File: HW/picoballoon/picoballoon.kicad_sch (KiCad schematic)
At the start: 23 parts, among them J1 EXT_DEBUGGER

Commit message: aprs test board
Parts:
- added R10, R11, R12, R13: 10k, symbol Device:R
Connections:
- net +3.3V: now also R10.1, R11.1, R12.1, R13.1
- net GNSS_EXTINT: now also MCXL14x2.5 (P0_13); no longer MCXL14x2.45 (P1_1)
- net GNSS_RESET: now also MCXL14x2.4 (P0_12); no longer MCXL14x2.44 (P1_0)
- net SCLK: now also MCXL14x2.45 (P1_1); no longer MCXL14x2.54 (P1_17)
- net nIRQ: now also MCXL14x2.48 (P1_12); no longer MCXL14x2.57 (P1_20)
- net nSEL: now also MCXL14x2.44 (P1_0); no longer MCXL14x2.56 (P1_19)
- net SDA_TEMP: now reaches MCXL14x2.10 (P0_18)
- net SDA_TEMP: now also R10.2
- net SCL_TEMP: now reaches MCXL14x2.11 (P0_19)
- net SCL_TEMP: now also R11.2
- net LED: now reaches D2.1 (K), MCXL14x2.16 (P0_20)
- net MI: now reaches MCXL14x2.46 (P1_2)
- net MO: now reaches MCXL14x2.47 (P1_3)
- net MO: now also R9.2
- net GNSS_TX: now reaches MCXL14x2.61 (P0_0)
- net GNSS_RX: now reaches MCXL14x2.62 (P0_1)
- net SCL renamed GNSS_SCL
- net SDA renamed GNSS_SDA
- net SI: no longer names the net of MCXL14x2.53 (P1_16)
- net SO: no longer names the net of MCXL14x2.55 (P1_18)
- net SO: no longer R9.2
- new net SCL_SENS: MCXL14x2.57 (P1_20), R13.2
- new net SDA_SENS: MCXL14x2.56 (P1_19), R12.2
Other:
- sheet GNSS ports: added EN, EXTINT, RESET, RX, TX; removed GNSS_EN, GNSS_EXTINT, GNSS_RESET
- sheet sensors ports: added SCL_TEMP, SDA_TEMP; removed none
- moved on the sheet: D2, J1, R1, R3, R4, R5, R9

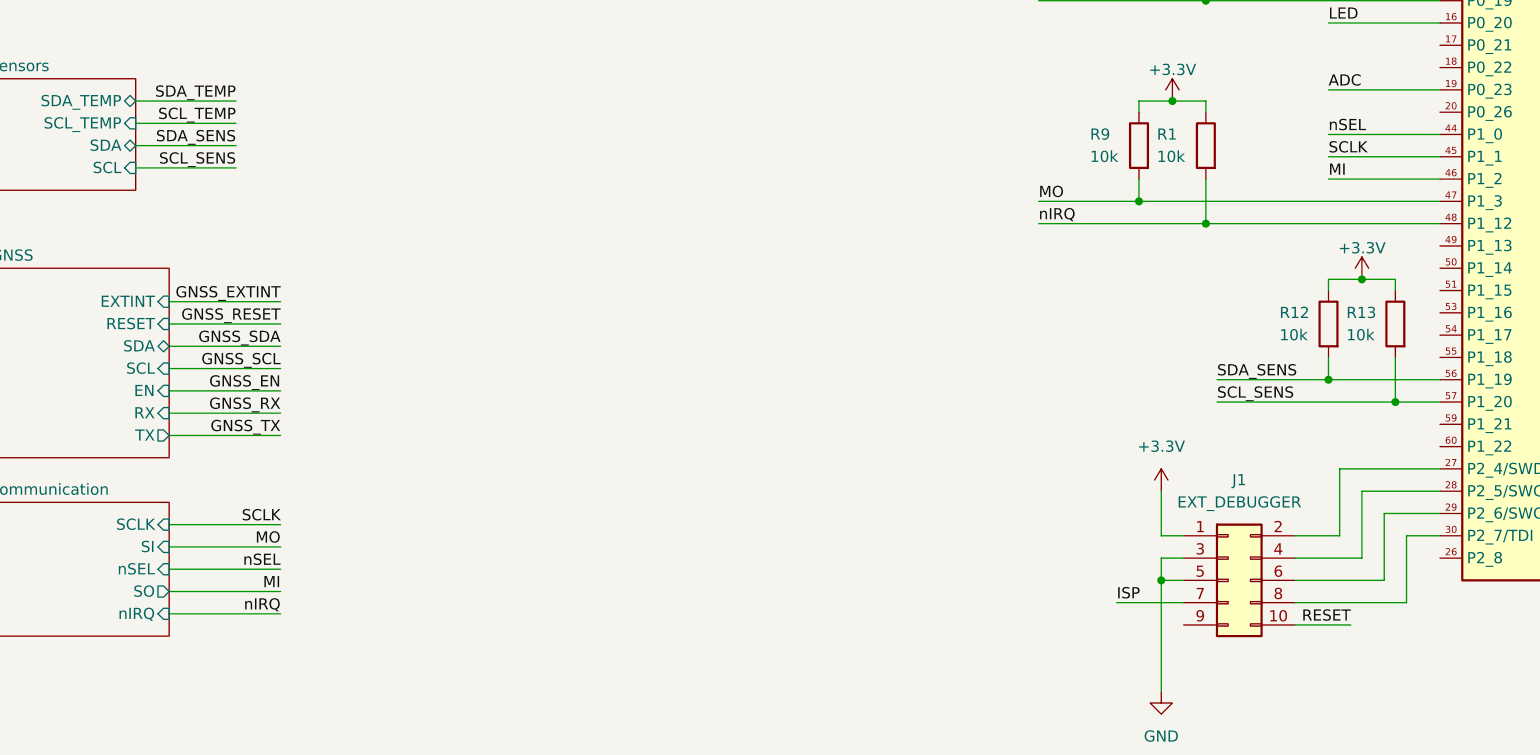
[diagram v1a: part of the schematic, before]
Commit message: some devices replaced
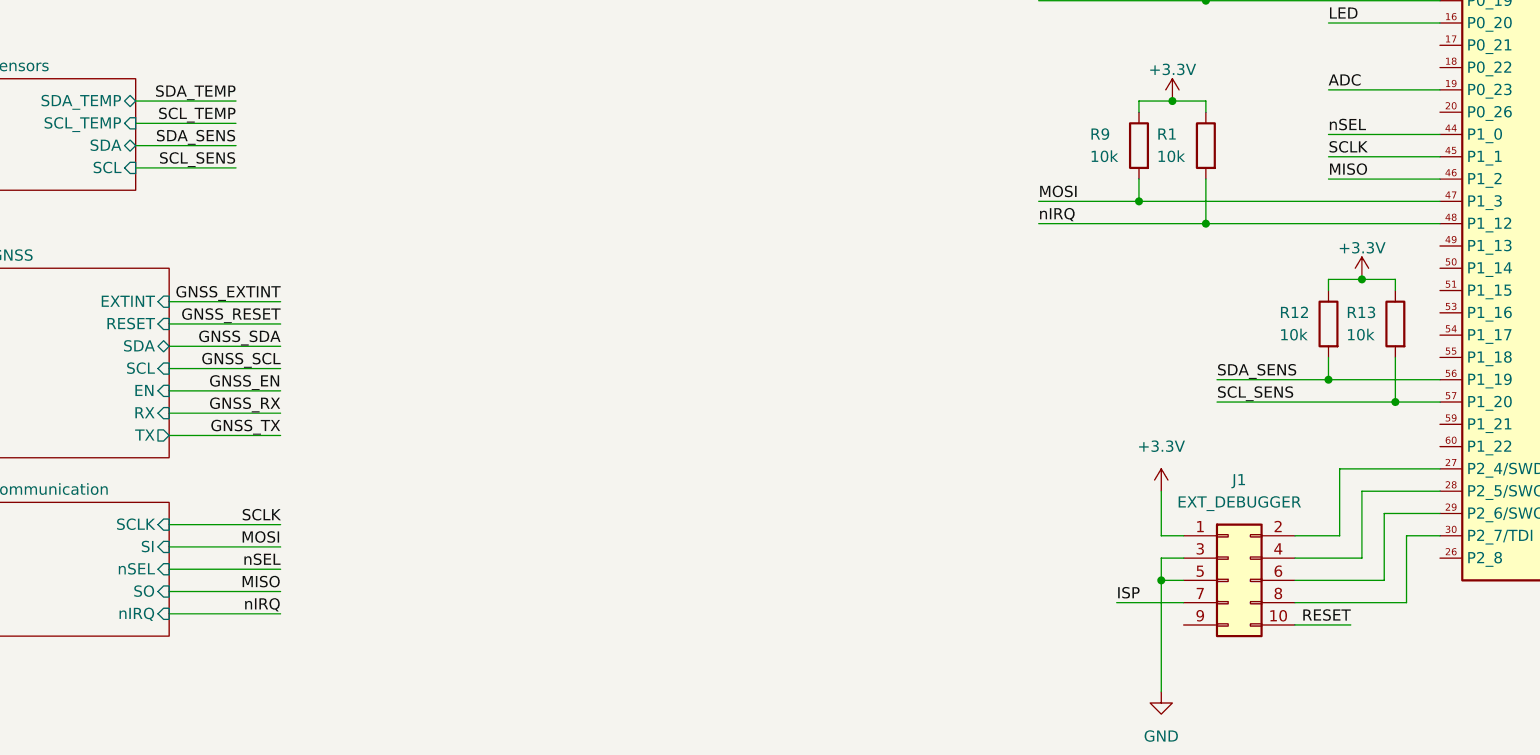
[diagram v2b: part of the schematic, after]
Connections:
- net MI renamed MISO
- net MO renamed MOSI
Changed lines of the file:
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@@
 	(wire
 		(pts
-			(xy 45.72 135.89) (xy 58.42 135.89)
-		)
-		(stroke
-			(width 0)
-			(type default)
-		)
-	)
-	(wire
-		(pts
 			(xy 120.65 170.18) (xy 120.65 168.91)
 		)
@@
 	(wire
 		(pts
+			(xy 45.72 130.81) (xy 58.42 130.81)
+		)
+		(stroke
+			(width 0)
+			(type default)
+		)
+	)
+	(wire
+		(pts
 			(xy 177.8 40.64) (xy 190.5 40.64)
 		)
@@
 	(wire
 		(pts
-			(xy 45.72 130.81) (xy 58.42 130.81)
-		)
-		(stroke
-			(width 0)
-			(type default)
-		)
-	)
-	(wire
-		(pts
 			(xy 259.08 124.46) (xy 275.59 124.46)
 		)
@@
 	(wire
 		(pts
+			(xy 45.72 135.89) (xy 58.42 135.89)
+		)
+		(stroke
+			(width 0)
+			(type default)
+		)
+	)
+	(wire
+		(pts
 			(xy 144.78 68.58) (xy 163.83 68.58)
 		)
@@
 		)
 	)
-	(label "MO"
+	(label "MOSI"
 		(at 58.42 130.81 180)
 		(fields_autoplaced yes)
@@
 		)
 	)
-	(label "MI"
+	(label "MISO"
 		(at 58.42 135.89 180)
 		(fields_autoplaced yes)
@@
 		)
 	)
-	(label "MO"
+	(label "MOSI"
 		(at 144.78 91.44 0)
 		(fields_autoplaced yes)
@@
 		)
 	)
-	(label "MI"
+	(label "MISO"
 		(at 177.8 88.9 0)
 		(fields_autoplaced yes)
@@
 			)
 		)
-		(pin "SO" output
+		(pin "SO" input
 			(at 45.72 135.89 0)
 			(effects

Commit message: pcb
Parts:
- C18, C19, C20, C21, C22, C23, C24, C25, C26, C27, C28, C29: footprint (none) -> Capacitor_SMD:C_0603_1608Metric_Pad1.08x0.95mm_HandSolder
- D2: footprint (none) -> LED_SMD:LED_0603_1608Metric_Pad1.05x0.95mm_HandSolder
- FB3: footprint (none) -> Library:BLM21AG102BH1J
- J1: footprint (none) -> Connector_PinHeader_1.27mm:PinHeader_2x05_P1.27mm_Vertical
- L4, L5: footprint (none) -> Inductor_SMD:L_0603_1608Metric_Pad1.05x0.95mm_HandSolder
- MCXL14x2: footprint (none) -> Package_QFP:LQFP-64-1EP_10x10mm_P0.5mm_EP5x5mm
- R1, R10, R11, R12, R13, R3, R4, R5, R9: footprint (none) -> Resistor_SMD:R_0603_1608Metric_Pad0.98x0.95mm_HandSolder
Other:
- sheet GNSS ports: added none; removed EN
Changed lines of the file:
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@@
 	(wire
 		(pts
-			(xy 45.72 115.57) (xy 58.42 115.57)
+			(xy 45.72 113.03) (xy 58.42 113.03)
 		)
 		(stroke
@@
 	(wire
 		(pts
-			(xy 128.27 55.88) (xy 134.62 55.88)
+			(xy 45.72 115.57) (xy 58.42 115.57)
 		)
 		(stroke
@@
 	(wire
 		(pts
-			(xy 156.21 91.44) (xy 190.5 91.44)
+			(xy 128.27 55.88) (xy 134.62 55.88)
 		)
 		(stroke
@@
 	(wire
 		(pts
-			(xy 186.69 129.54) (xy 190.5 129.54)
+			(xy 156.21 91.44) (xy 190.5 91.44)
 		)
 		(stroke
@@
 	(wire
 		(pts
-			(xy 45.72 102.87) (xy 58.42 102.87)
+			(xy 186.69 129.54) (xy 190.5 129.54)
 		)
 		(stroke
@@
 	(wire
 		(pts
-			(xy 233.68 55.88) (xy 234.95 55.88)
+			(xy 45.72 102.87) (xy 58.42 102.87)
 		)
 		(stroke
@@
 	(wire
 		(pts
-			(xy 45.72 118.11) (xy 58.42 118.11)
+			(xy 233.68 55.88) (xy 234.95 55.88)
 		)
 		(stroke
@@
 	(wire
 		(pts
-			(xy 45.72 113.03) (xy 58.42 113.03)
-		)
-		(stroke
-			(width 0)
-			(type default)
-		)
-	)
-	(wire
-		(pts
 			(xy 233.68 127) (xy 240.03 127)
 		)
@@
 		)
 	)
-	(label "GNSS_EN"
-		(at 58.42 113.03 180)
-		(fields_autoplaced yes)
-		(effects
-			(font
-				(size 1.27 1.27)
-			)
-			(justify right bottom)
-		)
-	)
 	(label "MOSI"
 		(at 58.42 130.81 180)
@@
 	)
 	(label "GNSS_TX"
-		(at 58.42 118.11 180)
+		(at 58.42 115.57 180)
 		(fields_autoplaced yes)
 		(effects
@@
 	)
 	(label "GNSS_RX"
-		(at 58.42 115.57 180)
+		(at 58.42 113.03 180)
 		(fields_autoplaced yes)
 		(effects
@@
 			)
 		)
-		(property "Footprint" ""
+		(property "Footprint" "Package_QFP:LQFP-64-1EP_10x10mm_P0.5mm_EP5x5mm"
 			(at 232.41 62.23 90)
 			(effects
@@
 			)
 		)
-		(property "Footprint" ""
+		(property "Footprint" "LED_SMD:LED_0603_1608Metric_Pad1.05x0.95mm_HandSolder"
 			(at 128.27 46.99 0)
 			(effects
@@
 			)
 		)
-		(property "Footprint" ""
+		(property "Footprint" "Capacitor_SMD:C_0603_1608Metric_Pad1.08x0.95mm_HandSolder"
 			(at 60.6552 177.8 0)
 			(effects
@@
 			)
 		)
-		(property "Footprint" ""
+		(property "Footprint" "Resistor_SMD:R_0603_1608Metric_Pad0.98x0.95mm_HandSolder"
 			(at 130.048 36.83 90)
 			(effects
@@
 			)
 		)
-		(property "Footprint" ""
+		(property "Footprint" "Resistor_SMD:R_0603_1608Metric_Pad0.98x0.95mm_HandSolder"
 			(at 171.958 41.91 90)
 			(effects
@@
 			)
 		)
-		(property "Footprint" ""
+		(property "Footprint" "Resistor_SMD:R_0603_1608Metric_Pad0.98x0.95mm_HandSolder"
 			(at 157.988 59.69 90)
 			(effects
@@
 			)
 		)
-		(property "Footprint" ""
+		(property "Footprint" "Capacitor_SMD:C_0603_1608Metric_Pad1.08x0.95mm_HandSolder"
 			(at 147.0152 177.8 0)
 			(effects
@@
 			)
 		)
-		(property "Footprint" ""
+		(property "Footprint" "Capacitor_SMD:C_0603_1608Metric_Pad1.08x0.95mm_HandSolder"
 			(at 98.7552 177.8 0)
 			(effects
@@
 			)
 		)
-		(property "Footprint" ""
+		(property "Footprint" "Capacitor_SMD:C_0603_1608Metric_Pad1.08x0.95mm_HandSolder"
 			(at 73.3552 177.8 0)
 			(effects
@@
 			)
 		)
-		(property "Footprint" ""
+		(property "Footprint" "Resistor_SMD:R_0603_1608Metric_Pad0.98x0.95mm_HandSolder"
 			(at 179.578 105.41 90)
 			(effects
@@
 			)
 		)
-		(property "Footprint" ""
+		(property "Footprint" "Capacitor_SMD:C_0603_1608Metric_Pad1.08x0.95mm_HandSolder"
 			(at 22.5552 177.8 0)
 			(effects
@@
 			)
 		)
-		(property "Footprint" ""
+		(property "Footprint" "Connector_PinHeader_1.27mm:PinHeader_2x05_P1.27mm_Vertical"
 			(at 166.37 134.62 0)
 			(effects
@@
 			)
 		)
-		(property "Footprint" ""
+		(property "Footprint" "Inductor_SMD:L_0603_1608Metric_Pad1.05x0.95mm_HandSolder"
 			(at 254 104.14 0)
 			(effects
@@
 			)
 		)
-		(property "Footprint" ""
+		(property "Footprint" "Capacitor_SMD:C_0603_1608Metric_Pad1.08x0.95mm_HandSolder"
 			(at 86.0552 177.8 0)
 			(effects
@@
 			)
 		)
-		(property "Footprint" ""
+		(property "Footprint" "Capacitor_SMD:C_0603_1608Metric_Pad1.08x0.95mm_HandSolder"
 			(at 159.7152 177.8 0)
 			(effects
@@
 			)
 		)
-		(property "Footprint" ""
+		(property "Footprint" "Capacitor_SMD:C_0603_1608Metric_Pad1.08x0.95mm_HandSolder"
 			(at 47.9552 177.8 0)
 			(effects
@@
 			)
 		)
-		(property "Footprint" ""
+		(property "Footprint" "Capacitor_SMD:C_0603_1608Metric_Pad1.08x0.95mm_HandSolder"
 			(at 260.0452 113.03 0)
 			(effects
@@
 			)
 		)
-		(property "Footprint" ""
+		(property "Footprint" "Capacitor_SMD:C_0603_1608Metric_Pad1.08x0.95mm_HandSolder"
 			(at 121.6152 177.8 0)
 			(effects
@@
 			)
 		)
-		(property "Footprint" ""
+		(property "Footprint" "Library:BLM21AG102BH1J"
 			(at 133.35 170.688 90)
 			(effects
@@
 			)
 		)
-		(property "Footprint" ""
+		(property "Footprint" "Capacitor_SMD:C_0603_1608Metric_Pad1.08x0.95mm_HandSolder"
 			(at 35.2552 177.8 0)
 			(effects
@@
 			)
 		)
-		(property "Footprint" ""
+		(property "Footprint" "Resistor_SMD:R_0603_1608Metric_Pad0.98x0.95mm_HandSolder"
 			(at 165.608 85.09 90)
 			(effects
@@
 			)
 		)
-		(property "Footprint" ""
+		(property "Footprint" "Resistor_SMD:R_0603_1608Metric_Pad0.98x0.95mm_HandSolder"
 			(at 164.338 41.91 90)
 			(effects
@@
 			)
 		)
-		(property "Footprint" ""
+		(property "Footprint" "Resistor_SMD:R_0603_1608Metric_Pad0.98x0.95mm_HandSolder"
 			(at 157.988 85.09 90)
 			(effects
@@
 			)
 		)
-		(property "Footprint" ""
+		(property "Footprint" "Resistor_SMD:R_0603_1608Metric_Pad0.98x0.95mm_HandSolder"
 			(at 187.198 105.41 90)
 			(effects
@@
 			)
 		)
-		(property "Footprint" ""
+		(property "Footprint" "Resistor_SMD:R_0603_1608Metric_Pad0.98x0.95mm_HandSolder"
 			(at 165.608 59.69 90)
 			(effects
@@
 			)
 		)
-		(property "Footprint" ""
+		(property "Footprint" "Capacitor_SMD:C_0603_1608Metric_Pad1.08x0.95mm_HandSolder"
 			(at 260.0452 133.35 0)
 			(effects
@@
 			)
 		)
-		(property "Footprint" ""
+		(property "Footprint" "Inductor_SMD:L_0603_1608Metric_Pad1.05x0.95mm_HandSolder"
 			(at 254 124.46 0)
 			(effects
@@
 	(sheet
 		(at 25.4 99.06)
-		(size 20.32 21.59)
+		(size 20.32 20.32)
 		(fields_autoplaced yes)
 		(stroke
@@
 		)
 		(property "Sheetfile" "GNSS.kicad_sch"
-			(at 25.4 121.2346 0)
+			(at 25.4 119.9646 0)
 			(effects
 				(font
@@
 			)
 		)
-		(pin "EN" input
-			(at 45.72 113.03 0)
-			(effects
-				(font
-					(size 1.27 1.27)
-				)
-				(justify right)
-			)
-		)
 		(pin "EXTINT" input
 			(at 45.72 102.87 0)
@@
 		)
 		(pin "TX" output
-			(at 45.72 118.11 0)
+			(at 45.72 115.57 0)
 			(effects
 				(font
@@
 		)
 		(pin "RX" input
-			(at 45.72 115.57 0)
+			(at 45.72 113.03 0)
 			(effects
 				(font

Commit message: picoballoon pcb
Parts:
- added C12: 100n, Capacitor_SMD:C_0603_1608Metric_Pad1.08x0.95mm_HandSolder, symbol Device:C
- added R6: 10k, Resistor_SMD:R_0603_1608Metric_Pad0.98x0.95mm_HandSolder, symbol Device:R
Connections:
- net +3.3V: now also R6.1
- net GND: now also C12.2
- net RESET: now also C12.1, R6.2

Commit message: test points
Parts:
- added TP1: +3.3VA_TP, TestPoint:TestPoint_Pad_D2.0mm, symbol Connector:TestPoint
- added TP10, TP9: GND, TestPoint:TestPoint_Pad_D2.0mm, symbol Connector:TestPoint
- added TP2: +3.3V_TP, TestPoint:TestPoint_Pad_D2.0mm, symbol Connector:TestPoint
- added TP4: SDA_TEMP, TestPoint:TestPoint_Pad_D2.0mm, symbol Connector:TestPoint
- added TP5: SCL_TEMP, TestPoint:TestPoint_Pad_D2.0mm, symbol Connector:TestPoint
- added TP6: SCLK, TestPoint:TestPoint_Pad_D2.0mm, symbol Connector:TestPoint
- added TP7: MOSI, TestPoint:TestPoint_Pad_D2.0mm, symbol Connector:TestPoint
- added TP8: MISO, TestPoint:TestPoint_Pad_D2.0mm, symbol Connector:TestPoint
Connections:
- net +3.3V: now also TP2.1
- net +3.3VA: now also TP1.1
- net GND: now also TP10.1, TP9.1
- net MISO: now also TP8.1
- net MOSI: now also TP7.1
- net SCLK: now also TP6.1
- net SCL_TEMP: now also TP5.1
- net SDA_TEMP: now also TP4.1

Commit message: test points
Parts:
- renumbered C23 to C10, C24 to C11, C25 to C12, C26 to C13, C27 to C14, C12 to C15, C28 to C16, C29 to C17, C18 to C5, C19 to C6, C20 to C7, C21 to C8, C22 to C9, L4 to L2, L5 to L3, R13 to R10, R3 to R11, R6 to R2, R4 to R3, R5 to R4, R10 to R5, R11 to R6, R9 to R7, R1 to R8, R12 to R9
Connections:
- net SDN: now reaches MCXL14x2.26 (P2_8)
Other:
- sheet communication ports: added SDN; removed none
- moved on the sheet: J1

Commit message: mcxc
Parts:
- removed C16: 4.7u, Capacitor_SMD:C_0603_1608Metric_Pad1.08x0.95mm_HandSolder, symbol Device:C
- removed L2, L3: 4.7u, Inductor_SMD:L_0603_1608Metric_Pad1.05x0.95mm_HandSolder, symbol Device:L
- removed MCXL14x2: ~, Package_QFP:LQFP-64-1EP_10x10mm_P0.5mm_EP5x5mm, symbol MCU_NXP_MCX:MCX_L14x
- added C15, C37: 100n, Capacitor_SMD:C_0603_1608Metric_Pad1.08x0.95mm_HandSolder, symbol Device:C
- added IC1: MCXC141VLH, Package_QFP:LQFP-64-1EP_10x10mm_P0.5mm_EP5x5mm, symbol Library:MCXC141VLH
- added R12, R13, R15, R16: 10k, Resistor_SMD:R_0603_1608Metric_Pad0.98x0.95mm_HandSolder, symbol Device:R
- added R14: 1k, Resistor_SMD:R_0603_1608Metric_Pad0.98x0.95mm_HandSolder, symbol Device:R
- added R19: 0, Resistor_SMD:R_0603_1608Metric_Pad0.98x0.95mm_HandSolder, symbol Device:R
- C10, C6, C8: value 100n -> 1u
- C17: value 4.7u -> xx
- renumbered C15 to C16
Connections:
- net +3.3V: now also R10.2, R5.2, R6.2, R9.2, C37.1, IC1.3 (VDD_1), IC1.30 (VDD_2), IC1.48 (VDD_3), R13.1, R15.1; no longer R10.1, R5.1, R6.1, R9.1
- net +3.3VA: now also C15.1, IC1.13 (VDDA), IC1.14 (VREFH_VREFO)
- net ADC: now also R14.1
- net GND: now also C15.2, C37.2, IC1.15 (VREFL), IC1.16 (VSSA), IC1.31 (VSS_2), IC1.4 (VSS_1), IC1.47 (VSS_3), R12.2, R16.2, R19.1
- net GNSS_EXTINT: now also IC1.62 (PTD5)
- net GNSS_RESET: now also IC1.61 (PTD4/LLWU_P14)
- net GNSS_RX: now also IC1.64 (PTD7)
- net GNSS_SCL: now also TP5.1, IC1.2 (PTE1)
- net GNSS_SDA: now also TP4.1, IC1.1 (PTE0)
- net GNSS_TX: now also IC1.63 (PTD6/LLWU_P15)
- net LED: now also IC1.17 (PTE29)
- net MISO: now also R7.2, IC1.52 (PTC7)
- net MOSI: now also R8.2, IC1.51 (PTC6/LLWU_P10); no longer R7.2
- net RESET: now also IC1.34 (PTA20)
- net SCLK: now also IC1.50 (PTC5/LLWU_P9)
- net SCL_SENS: now also R6.1, IC1.35 (PTB0/LLWU_P5); no longer R10.2
- net SCL_TEMP: now also R10.1, IC1.37 (PTB2); no longer R6.2, TP5.1
- net SDA_SENS: now also R5.1, IC1.36 (PTB1); no longer R9.2
- net SDA_TEMP: now also R9.1, IC1.38 (PTB3); no longer R5.2, TP4.1
- net SDN: now also IC1.46 (PTC3/LLWU_P7)
- net nIRQ: now also IC1.53 (PTC8); no longer R8.2
- net nSEL: now also IC1.49 (PTC4/LLWU_P8)
- net SWD_DIO: now reaches J1.2 (Pin_2)
- net SWD_DIO: now also IC1.25 (PTA3), R15.2
- net SWD_CLK: now reaches J1.4 (Pin_4)
- net SWD_CLK: now also IC1.22 (PTA0), R16.1
- net ISP: no longer names the net of J1.7 (Pin_7)
- net VDD_CORE_1POV: no longer names the net of C17.1
- net VDD_CORE_1POV: now also IC1.9 (PTE20), R14.2
- new net: IC1.7 (PTE18), R12.1
- new net: IC1.26 (PTA4), R13.2, R19.2
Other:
- moved on the sheet: C12, C13, C14, C16, D2, FB3, J1, R11, R2, R3, R4, R7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

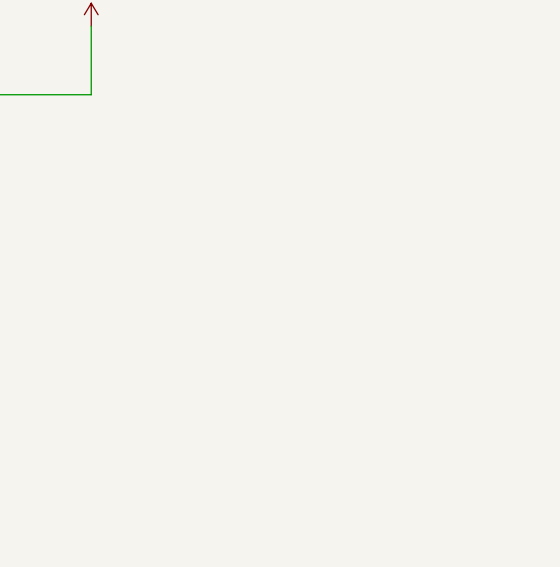
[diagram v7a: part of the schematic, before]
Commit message: mounting holes
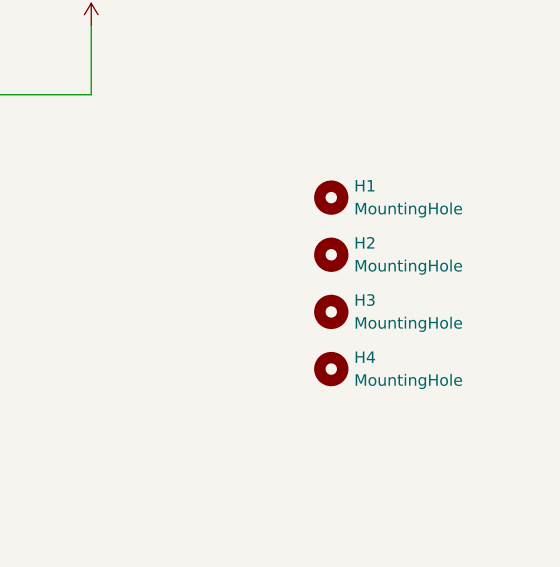
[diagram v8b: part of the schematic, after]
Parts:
- added H1, H2, H3, H4: MountingHole, MountingHole:MountingHole_2.1mm, symbol Mechanical:MountingHole
